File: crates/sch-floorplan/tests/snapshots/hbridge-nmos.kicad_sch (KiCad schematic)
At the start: 4 parts, among them Q1 Q_NMOS_GSD, Q2 Q_NMOS_GSD, Q3 Q_NMOS_GSD, Q4 Q_NMOS_GSD

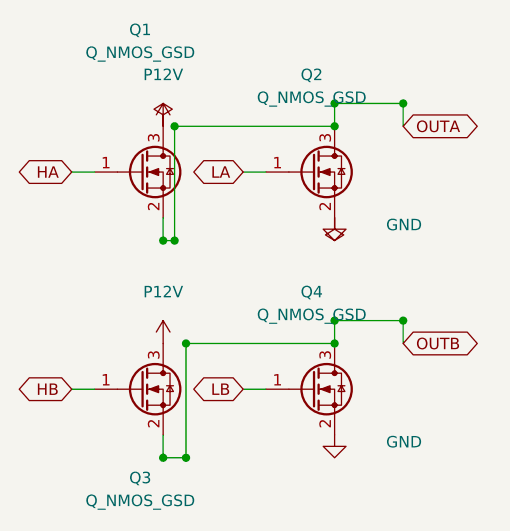
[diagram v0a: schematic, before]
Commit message: sch-doc: pick the smallest standard page from an A5-first ladder
A four-part circuit on A4 is a drawing stranded in one corner of an
empty sheet; the critic scored that a point worse than the snug custom
page it replaced. Starting the ladder at A5 keeps the frame close to
the content while every sheet still lands on a size KiCad and a printer
recognise.

Re-blessed the five snapshots whose critic score held at or above their
pre-change score. grid-demo is left at its baseline: it renders 7 where
it used to render 9.

Claude-Session: https://claude.ai/code/session_01GyGRY43X8yBh8WS1tjEmFz
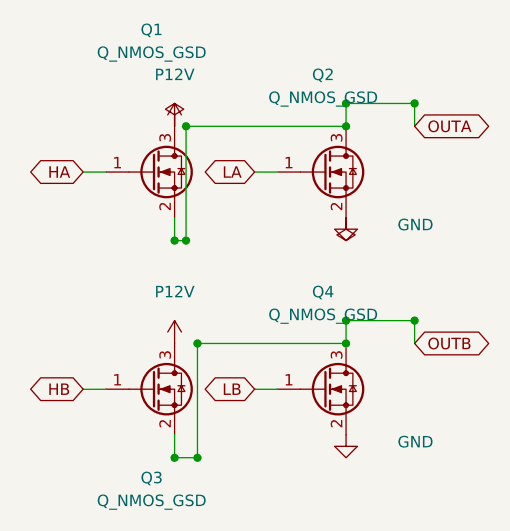
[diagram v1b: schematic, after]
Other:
- moved on the sheet: Q1, Q2, Q3, Q4
